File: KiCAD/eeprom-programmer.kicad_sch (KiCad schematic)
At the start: 1 part

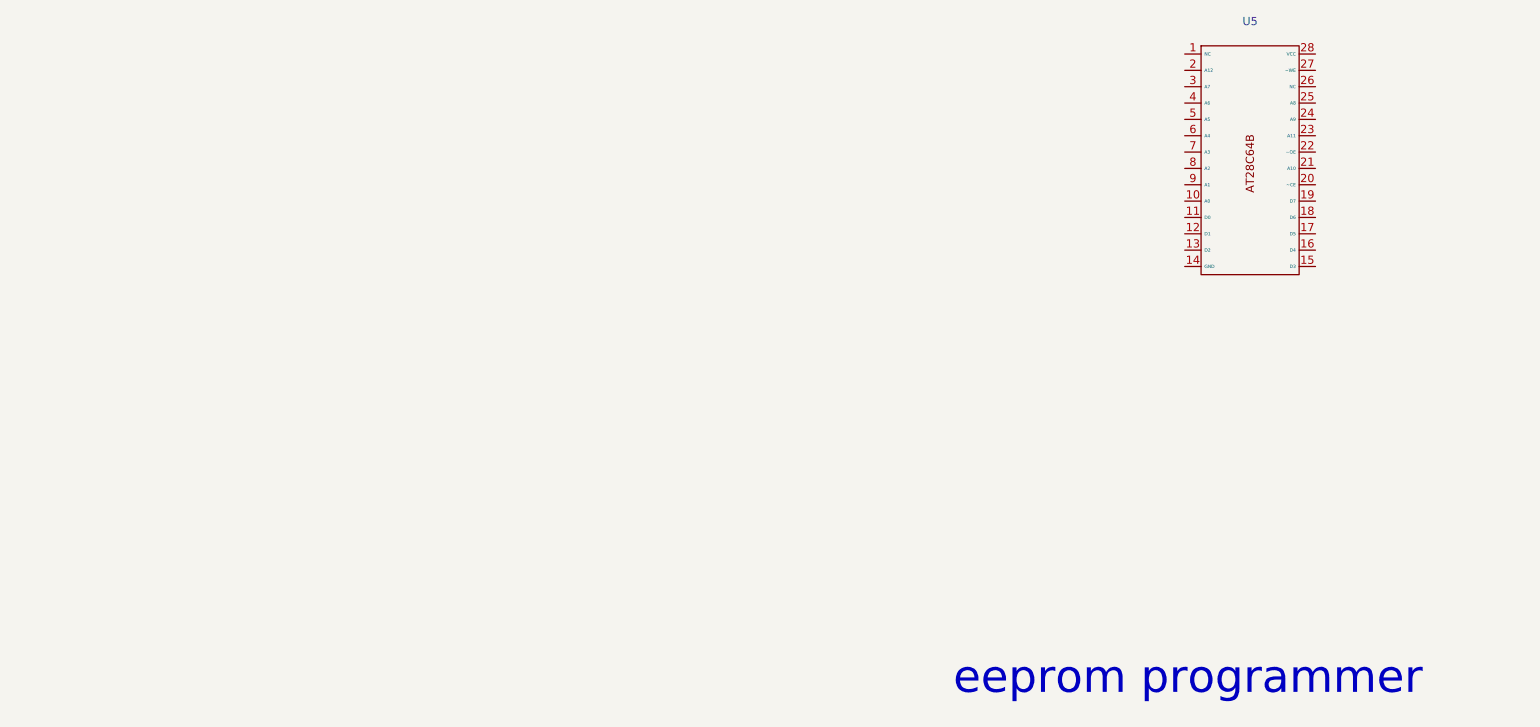
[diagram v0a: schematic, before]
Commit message: le travail avance sur eeProg.asm
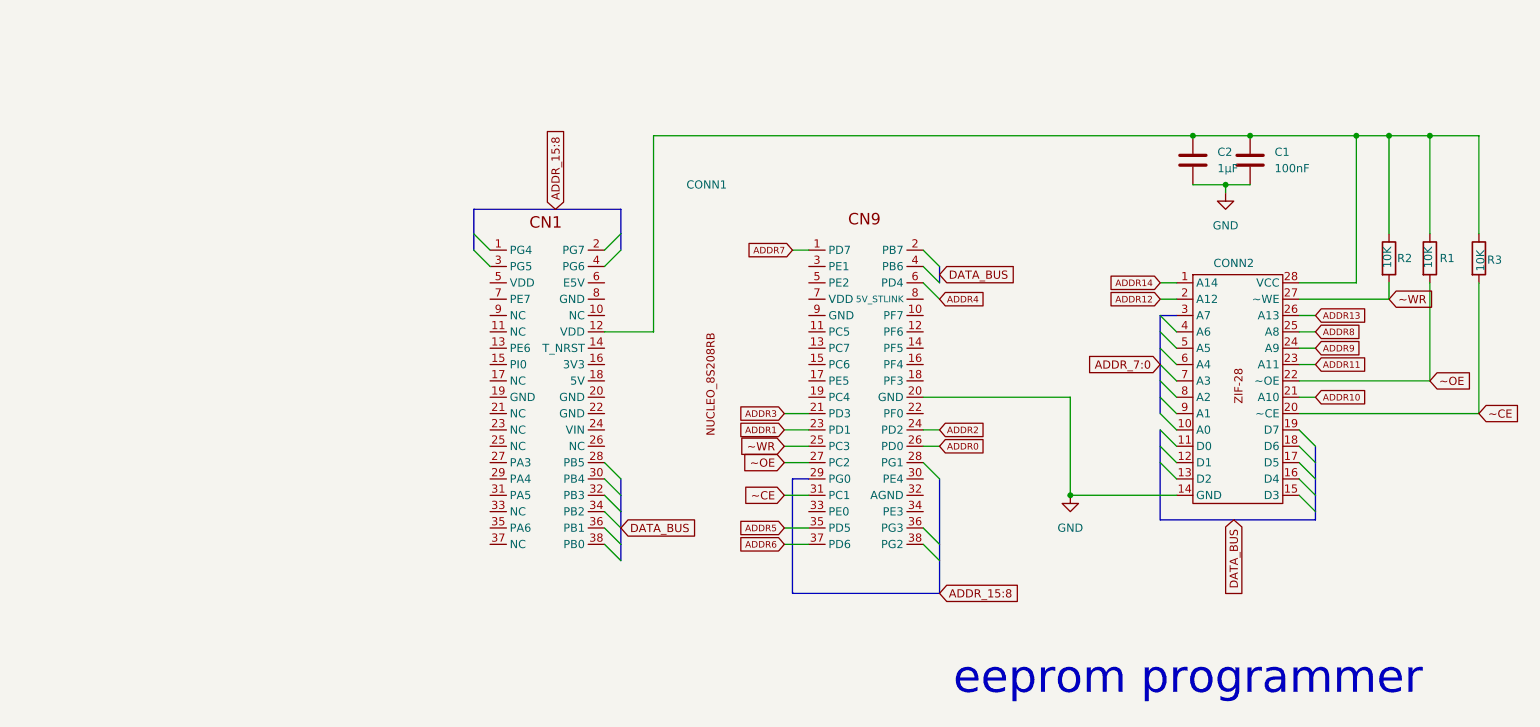
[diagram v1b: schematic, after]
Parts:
- removed U5: ~, symbol memory:AT28C64B
- added C1: 100nF, symbol Device:C
- added C2: 1µF, symbol Device:C
- added CONN1: ~, symbol nucleo_8s208rb:NUCLEO_CN1_CN9
- added CONN2: ~, symbol nucleo_8s208rb:ZIF-28
- added R1, R2, R3: 10K, symbol Device:R
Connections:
- new net: C1.1, C2.1, CONN1.12 (VDD), CONN2.28 (VCC), R1.1, R2.1, R3.1
- new net ADDR0: CONN1.26 (PD0)
- new net ADDR1: CONN1.23 (PD1)
- new net ADDR10: CONN2.21 (A10)
- new net ADDR11: CONN2.23 (A11)
- new net ADDR12: CONN2.2 (A12)
- new net ADDR13: CONN2.26 (A13)
- new net ADDR14: CONN2.1 (A14)
- new net ADDR2: CONN1.24 (VIN)
- new net ADDR3: CONN1.21 (PD3)
- new net ADDR5: CONN1.35 (PD5)
- new net ADDR6: CONN1.37 (PD6)
- new net ADDR7: CONN1.1 (PG4)
- new net ADDR8: CONN2.25 (A8)
- new net ADDR9: CONN2.24 (A9)
- new net GND: C1.2, C2.2, CONN1.20 (GND), CONN2.14 (GND)
- new net ~CE: CONN1.31 (PC1), CONN2.20 (~CE), R3.2
- new net ~OE: CONN1.27 (PC2), CONN2.22 (~OE), R1.2
- new net ~WR: CONN1.25 (PC3), CONN2.27 (~WE), R2.2

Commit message: travail sur le montage
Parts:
- removed C2: 1µF, symbol Device:C
- added C2: 10µF/25V, symbol Device:C_Polarized
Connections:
- net GND: now also C2.2
- net at C1.1, CONN2.28 (VCC), R1.1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: now also CONN1.7 (VDD), C2.1; no longer CONN1.12 (VDD)
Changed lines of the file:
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@@
+	)
+	(junction
+		(at 224.79 88.9)
+		(diameter 0)
+		(color 0 0 0 0)
 	)
 	(junction
@@
 		(color 0 0 0 0)
 	)
-	(junction
-		(at 224.79 88.9)
-		(diameter 0)
-		(color 0 0 0 0)
-	)
 	(bus_entry
 		(at 182.88 109.22)
@@
 	(wire
 		(pts
+			(xy 140.97 114.3) (xy 165.1 114.3)
+		)
+		(stroke
+			(width 0)
+			(type default)
+		)
+	)
+	(wire
+		(pts
 			(xy 182.88 137.16) (xy 185.42 137.16)
 		)
@@
 		)
 	)
+	(wire
+		(pts
+			(xy 140.97 88.9) (xy 140.97 114.3)
+		)
+		(stroke
+			(width 0)
+			(type default)
+		)
+	)
 	(bus
 		(pts
@@
 	(wire
 		(pts
-			(xy 140.97 119.38) (xy 140.97 88.9)
-		)
-		(stroke
-			(width 0)
-			(type default)
-		)
-	)
-	(wire
-		(pts
 			(xy 229.87 96.52) (xy 229.87 97.79)
 		)
@@
 		)
 	)
+	(wire
+		(pts
+			(xy 224.79 88.9) (xy 233.68 88.9)
+		)
+		(stroke
+			(width 0)
+			(type default)
+		)
+	)
 	(bus
 		(pts
@@
 		)
 	)
-	(wire
-		(pts
-			(xy 133.35 119.38) (xy 140.97 119.38)
-		)
-		(stroke
-			(width 0)
-			(type default)
-		)
-	)
 	(bus
 		(pts
@@
 		(pts
 			(xy 219.71 134.62) (xy 219.71 137.16)
-		)
-		(stroke
-			(width 0)
-			(type default)
-		)
-	)
-	(wire
-		(pts
-			(xy 224.79 88.9) (xy 233.68 88.9)
 		)
 		(stroke
@@
 	)
 	(symbol
-		(lib_id "Device:C")
-		(at 224.79 92.71 0)
-		(unit 1)
-		(exclude_from_sim no)
-		(in_bom yes)
-		(on_board yes)
-		(dnp no)
-		(fields_autoplaced yes)
-		(property "Reference" "C2"
-			(at 228.6 91.4399 0)
-			(effects
-				(font
-					(size 1.27 1.27)
-				)
-				(justify left)
-			)
-		)
-		(property "Value" "1µF"
-			(at 228.6 93.9799 0)
-			(effects
-				(font
-					(size 1.27 1.27)
-				)
-				(justify left)
-			)
-		)
-		(property "Footprint" ""
-			(at 225.7552 96.52 0)
-			(effects
-				(font
-					(size 1.27 1.27)
-				)
-				(hide yes)
-			)
-		)
-		(property "Datasheet" "~"
-			(at 224.79 92.71 0)
-			(effects
-				(font
-					(size 1.27 1.27)
-				)
-				(hide yes)
-			)
-		)
-		(property "Description" "Unpolarized capacitor"
-			(at 224.79 92.71 0)
-			(effects
-				(font
-					(size 1.27 1.27)
-				)
-				(hide yes)
-			)
-		)
-		(pin "1"
-		)
-		(pin "2"
-		)
-		(instances
-			(project ""
-				(path "/c7425404-c8c0-497e-bb4a-54a58f10b2cf"
-					(reference "C2")
-					(unit 1)
-				)
-			)
-		)
-	)
-	(symbol
 		(lib_id "power:GND")
 		(at 229.87 97.79 0)
@@
 	)
 	(symbol
+		(lib_id "Device:C_Polarized")
+		(at 224.79 92.71 0)
+		(unit 1)
+		(exclude_from_sim no)
+		(in_bom yes)
+		(on_board yes)
+		(dnp no)
+		(property "Reference" "C2"
+			(at 219.964 90.424 0)
+			(effects
+				(font
+					(size 1.27 1.27)
+				)
+				(justify left)
+			)
+		)
+		(property "Value" "10µF/25V"
+			(at 214.63 95.25 0)
+			(effects
+				(font
+					(size 1.27 1.27)
+				)
+				(justify left)
+			)
+		)
+		(property "Footprint" ""
+			(at 225.7552 96.52 0)
+			(effects
+				(font
+					(size 1.27 1.27)
+				)
+				(hide yes)
+			)
+		)
+		(property "Datasheet" "~"
+			(at 224.79 92.71 0)
+			(effects
+				(font
+					(size 1.27 1.27)
+				)
+				(hide yes)
+			)
+		)
+		(property "Description" "Polarized capacitor"
+			(at 224.79 92.71 0)
+			(effects
+				(font
+					(size 1.27 1.27)
+				)
+				(hide yes)
+			)
+		)
+		(pin "1"
+		)
+		(pin "2"
+		)
+		(instances
+			(project ""
+				(path "/c7425404-c8c0-497e-bb4a-54a58f10b2cf"
+					(reference "C2")
+					(unit 1)
+				)
+			)
+		)
+	)
+	(symbol
 		(lib_id "Device:C")
 		(at 233.68 92.71 0)
@@
 		(on_board yes)
 		(dnp no)
-		(fields_autoplaced yes)
 		(property "Reference" "C1"
-			(at 237.49 91.4399 0)
+			(at 234.442 90.678 0)
 			(effects
 				(font
@@
 		)
 		(property "Value" "100nF"
-			(at 237.49 93.9799 0)
-			(effects
-				(font
+			(at 234.95 95.25 0)
+			(effects
+				(font

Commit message: modifiation du circuit version 2 de eeprom-programmer
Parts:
- added CONN3: PLCC-32, symbol Memory_Flash:SST39SF010
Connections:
- net ADDR0 is gone; now on net A0: CONN1.26 (PD0)
- net ADDR1 is gone; now on net A1: CONN1.23 (PD1)
- net ADDR2 is gone; now on net A2: CONN1.24 (VIN)
- net ADDR3 is gone; now on net A3: CONN1.21 (PD3)
- net ADDR5 is gone; now on net A5: CONN1.35 (PD5)
- net ADDR6 is gone; now on net A6: CONN1.37 (PD6)
- net GND: now also CONN1.8 (GND), CONN3.16 (GND)
- net ~CE: now also CONN3.22 (CE)
- net ~OE: now also CONN3.24 (OE)
- net ~WR: now also CONN3.31 (PGM)
- net at C1.1, C2.1, CONN1.7 (VDD)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: now also CONN1.12 (VDD), CONN3.32 (VCC)
- net D7: now reaches CONN1.2 (PG7)
- net A3: now reaches CONN1.21 (PD3)
- net A16: now reaches CONN1.22 (PF0)
- net A1: now reaches CONN1.23 (PD1)
- net A2: now reaches CONN1.24 (VIN)
- net A0: now reaches CONN1.26 (PD0)
- net D5: now reaches CONN1.28 (PG1)
- net A13: now reaches CONN1.3 (PG5)
- net D4: now reaches CONN1.30 (PE4)
- net D3: now reaches CONN1.32 (PB3)
- net D2: now reaches CONN1.34 (PE3)
- net A5: now reaches CONN1.35 (PD5)
- net D1: now reaches CONN1.36 (PG3)
- net A6: now reaches CONN1.37 (PD6)
- net D0: now reaches CONN1.38 (PG2)
- net D6: now reaches CONN1.4 (PG6)
- net A4: now reaches CONN1.6 (PD4)
- net ADDR11: no longer names the net of CONN2.23 (A11)
- net ADDR12: no longer names the net of CONN2.2 (A12)
- net ADDR13: no longer names the net of CONN2.26 (A13)
- net ADDR14: no longer names the net of CONN2.1 (A14)
- net ADDR8: no longer names the net of CONN2.25 (A8)
- net ADDR9: no longer names the net of CONN2.24 (A9)
- new net A10: CONN1.38 (PG2)
- new net A11: CONN1.36 (PG3)
- new net A12: CONN1.1 (PG4)
- new net A14: CONN1.4 (PG6)
- new net A15: CONN1.2 (PG7)
- new net A9: CONN1.28 (PG1)
- no-connect marks 0 -> 2
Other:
- note added: "eeprom programmer version 2"
- note removed: "eeprom programmer"
- moved on the sheet: C1, C2, CONN1, CONN2, R1, R2, R3

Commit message: Modification au circuit, version 2.1
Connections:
- net A16: now also CONN1.33 (PE0)
- net at C1.1, C2.1, CONN1.12 (VDD)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: no longer CONN1.7 (VDD)
- net A18: now reaches CONN1.3 (PG5)
- net A19: now reaches CONN1.5 (VDD)
- new net A17: CONN1.34 (PE3)

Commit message: Mofication au circuit du programmeur, version 2.2
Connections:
- net A16: no longer CONN1.22 (PF0)
- net A17: now also CONN1.3 (PG5), CONN3.30 (NC); no longer CONN1.34 (PE3)
- net A18: now also CONN1.5 (VDD), CONN3.1 (NC); no longer CONN1.3 (PG5)
- net A19: now also CONN1.34 (PE3); no longer CONN1.5 (VDD)
- no-connect marks 2 -> 0
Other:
- note added: "eeprom programmer version 2.2"
- note removed: "eeprom programmer version 2"
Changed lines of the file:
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@@
+	)
+	(junction
+		(at 119.38 128.27)
+		(diameter 0)
+		(color 0 0 0 0)
 	)
 	(junction
@@
 		(color 0 0 0 0)
 	)
-	(no_connect
-		(at 227.33 130.81)
-	)
-	(no_connect
-		(at 227.33 133.35)
-	)
 	(bus_entry
 		(at 149.86 128.27)
@@
 	)
 	(bus_entry
+		(at 224.79 130.81)
+		(size 2.54 2.54)
+		(stroke
+			(width 0)
+			(type default)
+		)
+	)
+	(bus_entry
 		(at 113.03 100.33)
 		(size 2.54 -2.54)
@@
 	)
 	(bus_entry
+		(at 224.79 128.27)
+		(size 2.54 2.54)
+		(stroke
+			(width 0)
+			(type default)
+		)
+	)
+	(bus_entry
 		(at 224.79 120.65)
 		(size 2.54 2.54)
@@
 	(bus
 		(pts
+			(xy 224.79 125.73) (xy 224.79 128.27)
+		)
+		(stroke
+			(width 0)
+			(type default)
+		)
+	)
+	(bus
+		(pts
 			(xy 83.82 125.73) (xy 83.82 128.27)
 		)
@@
 	(bus
 		(pts
-			(xy 119.38 105.41) (xy 119.38 130.81)
+			(xy 119.38 105.41) (xy 119.38 128.27)
 		)
 		(stroke
@@
 	(bus
 		(pts
+			(xy 224.79 128.27) (xy 224.79 130.81)
+		)
+		(stroke
+			(width 0)
+			(type default)
+		)
+	)
+	(bus
+		(pts
 			(xy 119.38 130.81) (xy 119.38 133.35)
 		)
@@
 		)
 	)
+	(bus
+		(pts
+			(xy 119.38 128.27) (xy 119.38 130.81)
+		)
+		(stroke
+			(width 0)
+			(type default)
+		)
+	)
 	(wire
 		(pts
@@
 	(bus
 		(pts
+			(xy 115.57 128.27) (xy 119.38 128.27)
+		)
+		(stroke
+			(width 0)
+			(type default)
+		)
+	)
+	(bus
+		(pts
 			(xy 149.86 110.49) (xy 149.86 107.95)
 		)
@@
 		)
 	)
-	(text "eeprom programmer\nversion 2"
+	(text "eeprom programmer\nversion 2.2"
 		(exclude_from_sim no)
 		(at 178.562 171.958 0)
@@
 		)
 	)
-	(label "A16"
-		(at 113.03 123.19 0)
-		(effects
-			(font
-				(size 1.27 1.27)
-			)
-			(justify left bottom)
-		)
-	)
 	(label "A8"
 		(at 93.98 133.35 180)
@@
 	)
 	(label "A19"
-		(at 95.25 102.87 180)
-		(effects
-			(font
-				(size 1.27 1.27)
-			)
-			(justify right bottom)
+		(at 113.03 138.43 0)
+		(effects
+			(font
+				(size 1.27 1.27)
+			)
+			(justify left bottom)
 		)
 	)
@@
 	)
 	(label "A18"
-		(at 95.25 100.33 180)
+		(at 95.25 102.87 180)
 		(effects
 			(font
@@
 		)
 	)
+	(label "A18"
+		(at 227.33 133.35 180)
+		(effects
+			(font
+				(size 1.27 1.27)
+			)
+			(justify right bottom)
+		)
+	)
 	(label "A7"
 		(at 95.25 97.79 180)
@@
 	)
 	(label "A17"
-		(at 113.03 138.43 0)
-		(effects
-			(font
-				(size 1.27 1.27)
-			)
-			(justify left bottom)
+		(at 95.25 100.33 180)
+		(effects
+			(font
+				(size 1.27 1.27)
+			)
+			(justify right bottom)
 		)
 	)
@@
 		)
 	)
+	(label "A17"
+		(at 227.33 130.81 180)
+		(effects
+			(font
+				(size 1.27 1.27)
+			)
+			(justify right bottom)
+		)
+	)

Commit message: modfication mineure au montage de la cape.
Ajout d'un bouton RESET sur la cape.
Ajout d'un commteur de sélection VDD 3.3V|5V sur la cape.
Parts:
- added J1: NUCLEO JP3, symbol Connector:Conn_01x03_Socket
- added SW1: ~{RST}, symbol Switch:SW_MEC_5G
- added SW2: VDD select, symbol Switch:SW_SPDT
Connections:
- net GND: now also SW1.3 (B), SW1.4 (B)
- net ~{NRST}: now reaches CONN1.14 (PF5)
- net ~{NRST}: now also SW1.1 (A), SW1.2 (A)
- new net: J1.2 (Pin_2), SW2.2 (B)
- new net 3.3V: J1.1 (Pin_1), SW2.1 (A)
- new net 5V: J1.3 (Pin_3), SW2.3 (C)
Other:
- note added: "eeprom programmer version 2.3"
- note removed: "eeprom programmer version 2.2"

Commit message: Modification au circuit électronique. Remplacement du transistor ZTX749 par un P-MOSFET SI2305CD
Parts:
- added Q1: SI2305CD, symbol Simulation_SPICE:PMOS
- added R4: 1M, symbol Device:R
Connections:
- net at C1.1, C2.1, CONN2.28 (VCC)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: now also Q1.1 (D); no longer CONN1.12 (PF6)
- new net: CONN1.22 (PF0), Q1.2 (G), R4.2
- new net: CONN1.12 (PF6), Q1.3 (S), R4.1
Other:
- note added: "eeprom programmer version 2.4"
- note removed: "eeprom programmer version 2.3"
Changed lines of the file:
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@@
 	(generator_version "9.0")
 	(paper "A4")
-	(text "eeprom programmer\nversion 2.3"
+	(text "eeprom programmer\nversion 2.4"
 		(exclude_from_sim no)
 		(at 178.562 171.958 0)
@@
 	)
 	(junction
+		(at 133.35 87.63)
+		(diameter 0)
+		(color 0 0 0 0)
+	)
+	(junction
 		(at 199.39 80.01)
 		(diameter 0)
@@
 	)
 	(junction
-		(at 154.94 80.01)
+		(at 123.19 80.01)
 		(diameter 0)
 		(color 0 0 0 0)
@@
 	)
 	(junction
+		(at 154.94 80.01)
+		(diameter 0)
+		(color 0 0 0 0)
+	)
+	(junction
 		(at 160.02 87.63)
 		(diameter 0)
@@
 	(wire
 		(pts
+			(xy 71.12 80.01) (xy 123.19 80.01)
+		)
+		(stroke
+			(width 0)
+			(type default)
+		)
+	)
+	(wire
+		(pts
 			(xy 92.71 97.79) (xy 95.25 97.79)
 		)
@@
 	(wire
 		(pts
-			(xy 71.12 80.01) (xy 154.94 80.01)
-		)
-		(stroke
-			(width 0)
-			(type default)
-		)
-	)
-	(wire
-		(pts
 			(xy 63.5 110.49) (xy 71.12 110.49)
 		)
@@
 	(wire
 		(pts
+			(xy 138.43 80.01) (xy 154.94 80.01)
+		)
+		(stroke
+			(width 0)
+			(type default)
+		)
+	)
+	(wire
+		(pts
 			(xy 160.02 87.63) (xy 160.02 88.9)
 		)
@@
 	(wire
 		(pts
+			(xy 133.35 123.19) (xy 133.35 87.63)
+		)
+		(stroke
+			(width 0)
+			(type default)
+		)
+	)
+	(wire
+		(pts
 			(xy 91.44 130.81) (xy 95.25 130.81)
 		)
@@
 	(wire
 		(pts
+			(xy 123.19 80.01) (xy 128.27 80.01)
+		)
+		(stroke
+			(width 0)
+			(type default)
+		)
+	)
+	(wire
+		(pts
 			(xy 185.42 102.87) (xy 185.42 105.41)
 		)
@@
 		)
 	)
+	(wire
+		(pts
+			(xy 113.03 123.19) (xy 133.35 123.19)
+		)
+		(stroke
+			(width 0)
+			(type default)
+		)
+	)
 	(bus
 		(pts
@@
 		(pts
 			(xy 91.44 135.89) (xy 95.25 135.89)
+		)
+		(stroke
+			(width 0)
+			(type default)
+		)
+	)
+	(wire
+		(pts
+			(xy 123.19 87.63) (xy 133.35 87.63)
 		)
 		(stroke
@@
 				(justify left)
 				(hide yes)
+			)
+		)
+	)
+	(symbol
+		(lib_id "Simulation_SPICE:PMOS")
+		(at 133.35 82.55 270)
+		(mirror x)
+		(unit 1)
+		(exclude_from_sim no)
+		(in_bom yes)
+		(on_board yes)
+		(dnp no)
+		(fields_autoplaced yes)
+		(property "Reference" "Q1"
+			(at 133.35 73.66 90)
+			(effects
+				(font
+					(size 1.27 1.27)
+				)
+			)
+		)
+		(property "Value" "SI2305CD"
+			(at 133.35 76.2 90)
+			(effects
+				(font
+					(size 1.27 1.27)
+				)
+			)
+		)
+		(property "Footprint" ""
+			(at 135.89 77.47 0)
+			(effects
+				(font
+					(size 1.27 1.27)
+				)
+				(hide yes)
+			)
+		)
+		(property "Datasheet" "https://ngspice.sourceforge.io/docs/ngspice-html-manual/manual.xhtml#cha_MOSFETs"
+			(at 120.65 82.55 0)
+			(effects
+				(font
+					(size 1.27 1.27)
+				)
+				(hide yes)
+			)
+		)
+		(property "Description" "P-MOSFET transistor, drain/source/gate"
+			(at 133.35 82.55 0)
+			(effects
+				(font
+					(size 1.27 1.27)
+				)
+				(hide yes)
+			)
+		)
+		(property "Sim.Device" "PMOS"
+			(at 116.205 82.55 0)
+			(effects
+				(font
+					(size 1.27 1.27)
+				)
+				(hide yes)
+			)
+		)
+		(property "Sim.Type" "VDMOS"
+			(at 114.3 82.55 0)
+			(effects
+				(font
+					(size 1.27 1.27)
+				)
+				(hide yes)
+			)
+		)
+		(property "Sim.Pins" "1=D 2=G 3=S"
+			(at 118.11 82.55 0)
+			(effects
+				(font
+					(size 1.27 1.27)
+				)
+				(hide yes)
+			)
+		)
+		(pin "3"
+		)
+		(pin "1"
+		)
+		(pin "2"
+		)
+		(instances
+			(project ""
+				(path "/c7425404-c8c0-497e-bb4a-54a58f10b2cf"
+					(reference "Q1")
+					(unit 1)
+				)
 			)
 		)
@@
 					(unit 1)
 				)
+			)
+		)
+	)
+	(symbol
+		(lib_id "Device:R")
+		(at 123.19 83.82 0)
+		(unit 1)
+		(exclude_from_sim no)
+		(in_bom yes)
+		(on_board yes)
+		(dnp no)
+		(property "Reference" "R4"
+			(at 124.714 82.804 0)
+			(effects
+				(font
+					(size 1.27 1.27)
+				)
+				(justify left)
+			)
+		)
+		(property "Value" "1M"
+			(at 124.968 84.836 0)
+			(effects
+				(font
+					(size 1.27 1.27)
+				)
+				(justify left)
+			)
+		)
+		(property "Footprint" ""
+			(at 121.412 83.82 90)
+			(effects
+				(font
+					(size 1.27 1.27)
+				)
+				(hide yes)
+			)
+		)
+		(property "Datasheet" "~"
+			(at 123.19 83.82 0)
+			(effects
+				(font
+					(size 1.27 1.27)
+				)
+				(hide yes)
+			)
+		)
+		(property "Description" "Resistor"
+			(at 123.19 83.82 0)
+			(effects
+				(font
+					(size 1.27 1.27)
+				)
+				(hide yes)
+			)
+		)
+		(pin "2"
+		)
+		(pin "1"
+		)
+		(instances
+			(project ""
+				(path "/c7425404-c8c0-497e-bb4a-54a58f10b2cf"
+					(reference "R4")
+					(unit 1)
+				)

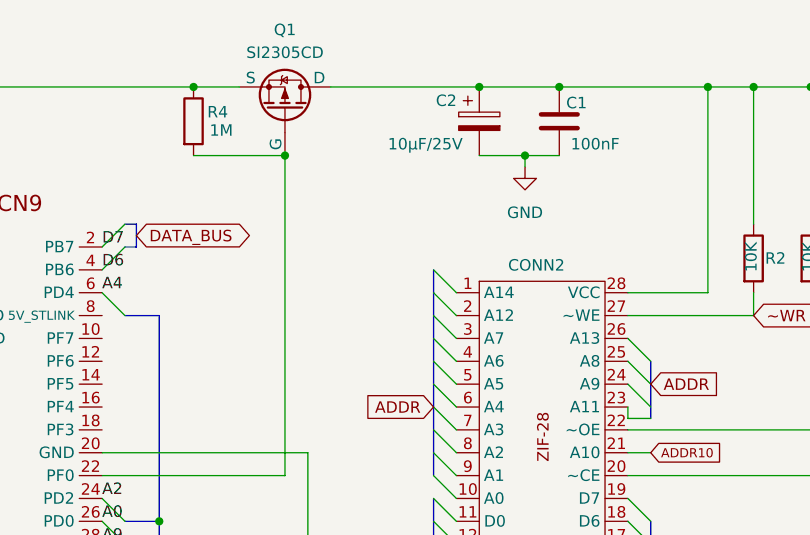
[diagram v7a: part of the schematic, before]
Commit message: correction d'un oublie dans le dessin du circuit
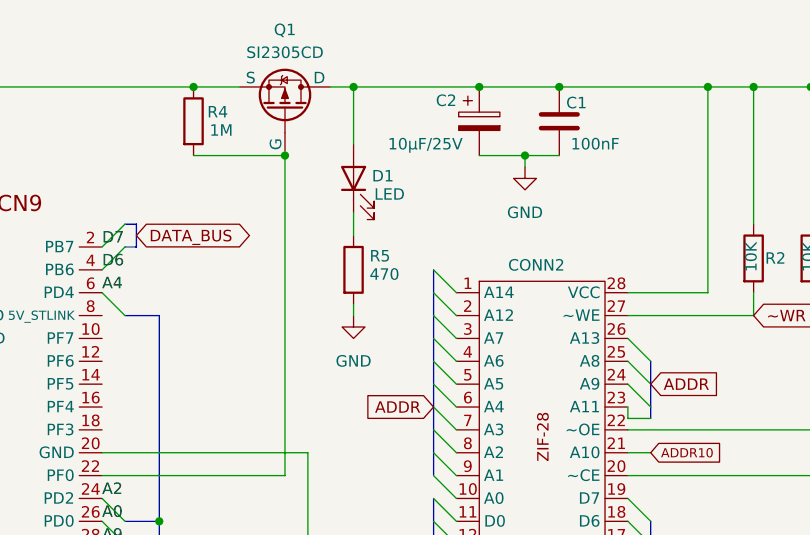
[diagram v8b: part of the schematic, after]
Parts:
- added D1: LED, symbol Device:LED
- added R5: 470, symbol Device:R
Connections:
- net GND: now also R5.2
- net at C1.1, C2.1, CONN2.28 (VCC)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: now also D1.2 (A)
- new net: D1.1 (K), R5.1
